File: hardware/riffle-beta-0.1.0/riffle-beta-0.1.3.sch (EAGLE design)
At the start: 46 parts, among them IC1 ATMEGA328P, IC3 CH340G, IC4 MCP1700-33, IC5 24AA128SN, IC6 MCP1700-33, J1 AYZ0202, U1 MCP73831T-2ACI/OT, X2 12MHz, X3 16 MHz

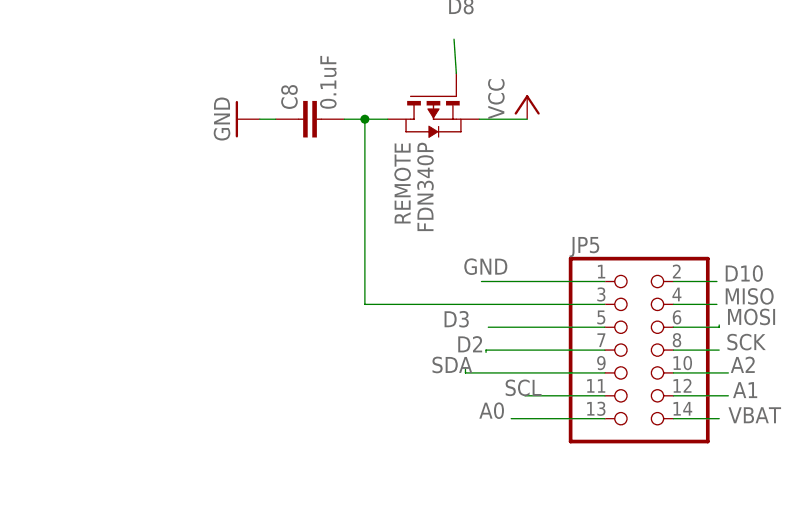
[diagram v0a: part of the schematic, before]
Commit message: tightened USB cutout; moved via away from left screw
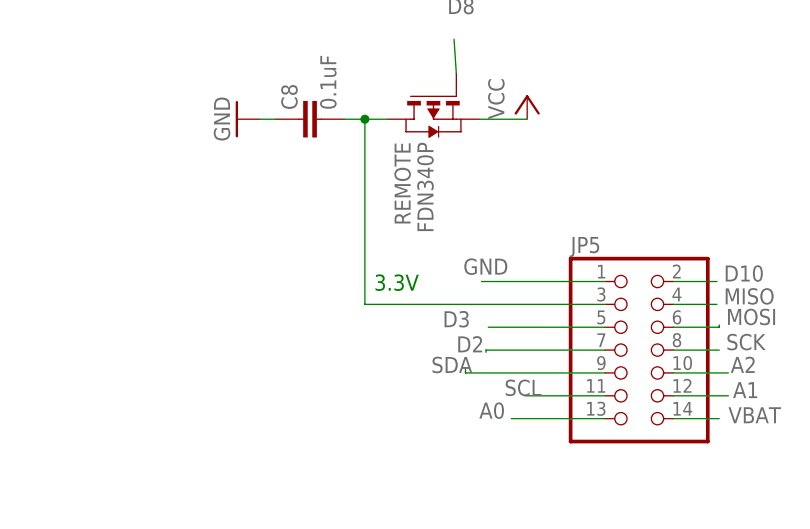
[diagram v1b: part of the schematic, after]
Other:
- note added: "3.3V"
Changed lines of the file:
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@@
 <setting verticaltext="up"/>
 </settings>
-<grid distance="0.01" unitdist="inch" unit="inch" style="lines" multiple="1" display="no" altdistance="0.01" altunitdist="inch" altunit="inch"/>
+<grid distance="0.1" unitdist="inch" unit="inch" style="lines" multiple="1" display="no" altdistance="0.01" altunitdist="inch" altunit="inch"/>
 <layers>
 <layer number="1" name="Top" color="4" fill="1" visible="no" active="no"/>
@@
 <plain>
 <text x="42.672" y="171.704" size="1.778" layer="91">i2c pullups</text>
+<text x="149.86" y="10.16" size="1.778" layer="91">3.3V</text>
 </plain>
 <instances>
